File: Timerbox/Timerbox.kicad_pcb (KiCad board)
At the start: 2 copper layers, 100 x 100 mm, 40 parts, among them CON1 AVR-ISP-6, IC1 ATTINY4313-P, K1 ROT, P1 CON, P2 BTN1, P3 BTN01, P4 RST, P5 BTN0, Q1 2N3904, U1 78L05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

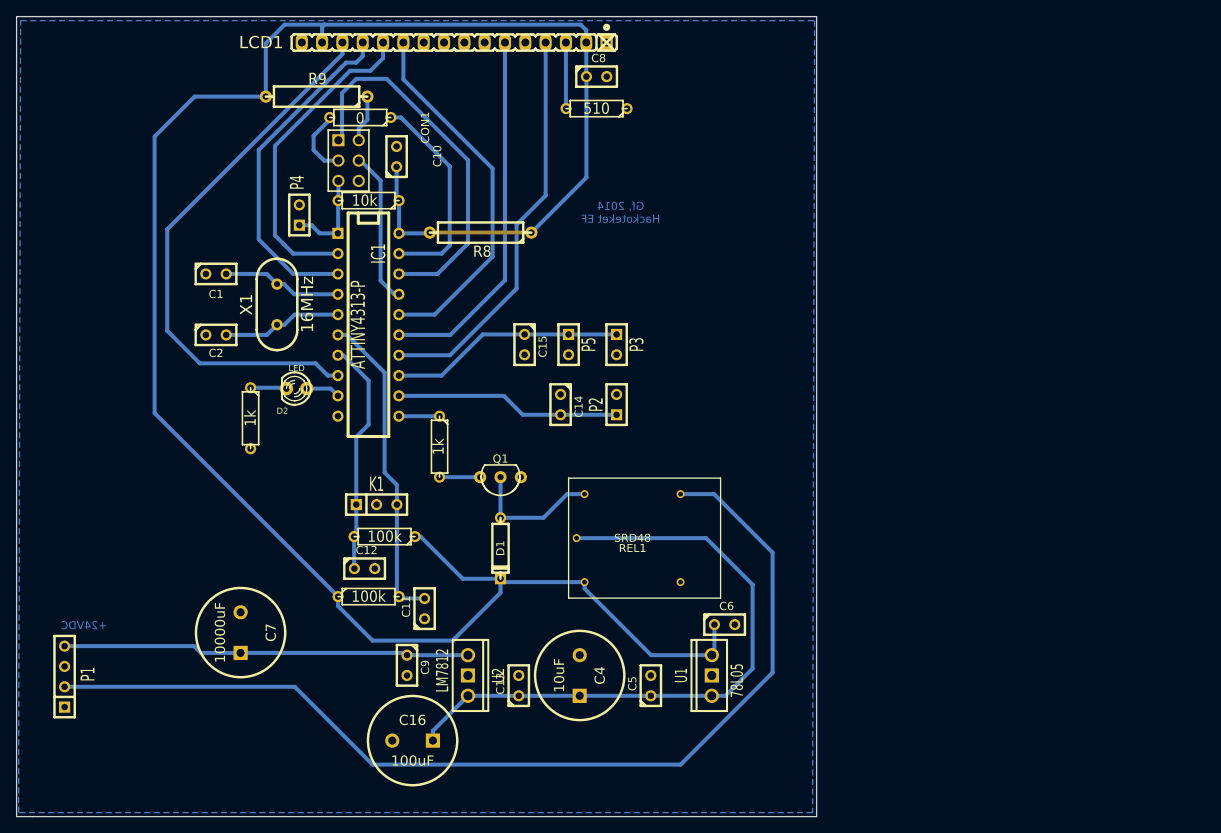
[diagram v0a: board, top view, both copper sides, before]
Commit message: Added some libs and some new circuits
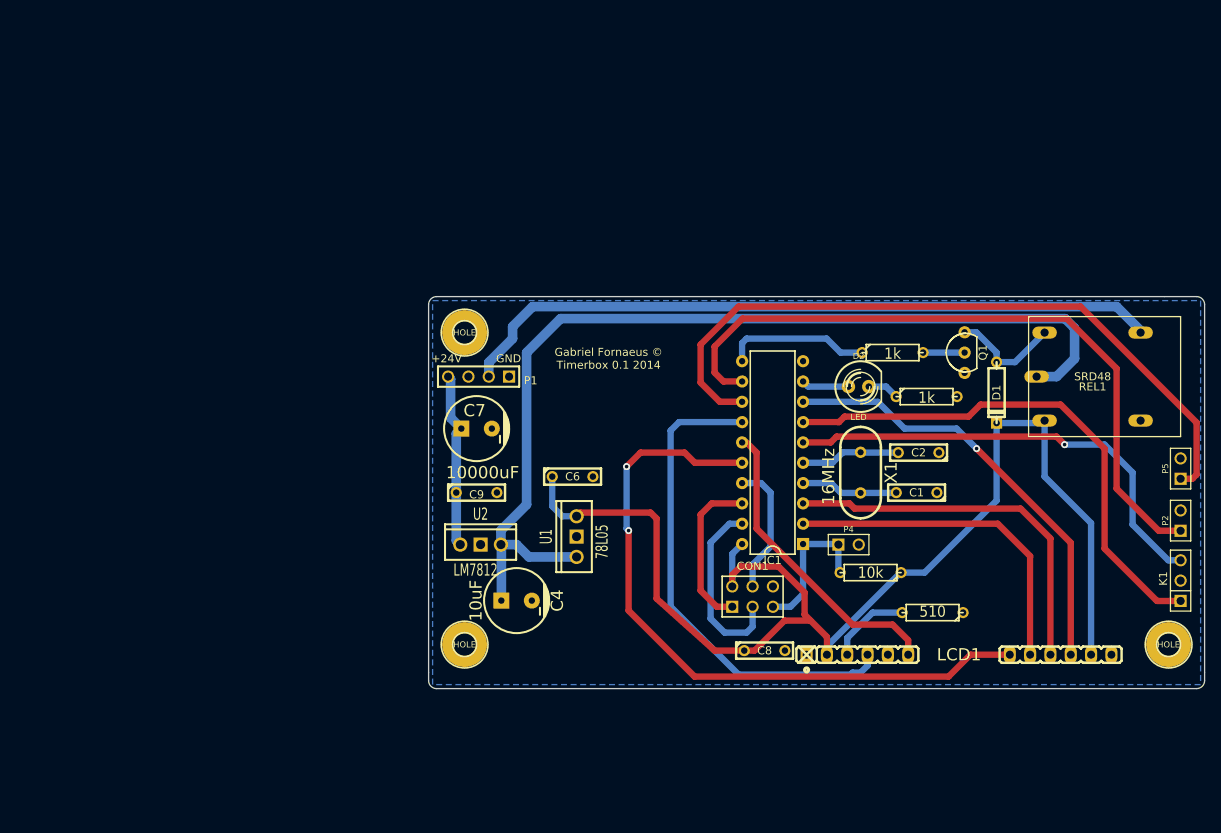
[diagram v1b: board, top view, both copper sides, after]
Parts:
- removed C10, C11, C12, C13, C14, C15, C5: 100nF, C1
- removed C16: 100uF, C2V10
- removed P3: BTN01, SIL-2
- removed R2, R3: 100k, R3
- removed R5: 0, R3
- removed R8, R9: 0, R5
- added HOLE: Val**, HOLE_28, F.Cu at (169.5, 97.5)
- added HOLE: Val**, HOLE_28, F.Cu at (169.5, 136.5)
- added HOLE: Val**, HOLE_28, F.Cu at (257.5, 136.5)
- C1, C2, C6, C8, C9: footprint C1 -> C2
- C4, C7: footprint C2V10 -> CP_8x13mm
- D2: footprint LED-3MM -> LED-5MM
- IC1: footprint DIP-20__300 -> DIL20_3
- K1: footprint SIL-3 -> PIN_ARRAY_3X1
- LCD1: footprint LV_1602-LCD-16pin -> LV_1602-LCD-6+6pin
- P1: footprint SIL-4 -> PIN_ARRAY_4x1
- P2, P4, P5: footprint SIL-2 -> PIN_ARRAY_2X1
- Q1: footprint TO92BCE_INLINE -> TO92CBE_INLINE
- moved LCD1 138.9 mm to (244.0, 153.0), turned to 0 degrees
- moved K1 100.9 mm to (259.0, 128.5), turned to 90 degrees
- moved C1 91.7 mm to (226.0, 117.5), turned to 180 degrees
- moved C2 89.0 mm to (226.2, 112.5), turned to 180 degrees
- moved R7 84.5 mm to (227.2, 105.5), turned to 0 degrees
- moved P4 80.1 mm to (217.5, 124.0), turned to 0 degrees
- moved R1 78.1 mm to (220.2, 127.5)
- moved P5 78.1 mm to (259.0, 114.5), turned to 90 degrees
- moved X1 75.9 mm to (219.0, 115.0), turned to 270 degrees
- moved R6 75.7 mm to (228.0, 132.5)
- moved C8 74.8 mm to (207.0, 137.2)
- moved CON1 74.3 mm to (205.5, 130.5), turned to 0 degrees
- moved P2 72.0 mm to (259.0, 121.0)
- moved D2 70.3 mm to (218.8, 104.2), turned to 0 degrees
- moved D1 65.0 mm to (236.0, 105.0)
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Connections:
- CON1 pad 2: N-000003 (its old number) -> +5V
- CON1 pad 3: N-0000012 -> /SCK
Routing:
- net +5V: track 261.9 -> 155.3 mm, vias 0 -> 1
- net N-000003: track 29.3 -> 89.6 mm
- net N-000002: track 28.2 -> 86.6 mm
- net +12V: track 79.3 -> 122.7 mm
- net /DB4: track 46.1 -> 86.0 mm, vias 0 -> 2
- net /RL1: track 126.8 -> 88.5 mm
- net /ROT1: track 29.4 -> 65.6 mm
- net +24V: track 50.9 -> 22.2 mm
- net /MISO: track 47.4 -> 20.1 mm
- net /ROT0: track 39.8 -> 57.7 mm, vias 0 -> 1
- net /DB7: track 68.8 -> 54.7 mm, vias 0 -> 1
- net N-000008: track 5.08 -> 18.2 mm
- net /RS: track 50.4 -> 61.4 mm
- net N-0000012: track 8.56 -> 0.00 mm
- net /E: track 45.8 -> 38.4 mm
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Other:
- board size 100 x 100 mm -> 97 x 49 mm
- net class Bigger added: clearance 0.254, trace_width 1.2, via_dia 0.889, via_drill 0.635
- net class Default: clearance 0.1 -> 0.254; trace_width 0.5 -> 0.8
- rule trace_clearance: 0.1 -> 0.254
- board text added: "+24V"
- board text added: "GND"
- board text added: "Gabriel Fornaeus © Timerbox 0.1 2014"
- board text removed: "+24VDC"
- board text removed: "Gf, 2014 Hackoteket EF"
